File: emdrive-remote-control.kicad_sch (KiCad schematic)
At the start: 44 parts, among them J1 Raspberry_Pi_2_3, J2 Screw_Terminal_01x06, J3 Conn_01x04, J4 Screw_Terminal_01x06, K1 Relay_SPST-NO, Q1 DMN61D8LQ, SW3 SW_Push, SW4 SW_Push, U1 ADS1015IDGS, U2 WS2801SO, U3 AP62150WU, U5 SN74HCS125, U6 MCP602, U7 BTS6143D

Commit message: Continues SCH, placed components on PCB
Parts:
- removed J4: Screw_Terminal_01x06, PrivateLibrary:Terminal_Block_SERIES 4115_5.08_Spring_6POS, symbol Connector:Screw_Terminal_01x06
- added Q2: MMBT3904, Package_TO_SOT_SMD:SOT-23, symbol Transistor_BJT:MMBT3904
- added R11, R12, R17, R18: 33k, Resistor_SMD:R_0603_1608Metric_Pad0.98x0.95mm_HandSolder, symbol Device:R
- renumbered SW3 to SW1, SW4 to SW2
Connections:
- net +12L: no longer K1.14
- net +12V: now also J2.1 (Pin_1), U7.3 (Vbb); no longer K1.13
- net +3.3V: now also J1.1 (3V3), J1.17 (3V3)
- net +5V: now also J1.2 (5V), J1.4 (5V)
- net GND: now also C10.1, C11.1, C12.1, C6.1, J1.14 (GND), J1.20 (GND), J1.25 (GND), J1.30 (GND), J1.34 (GND), J1.39 (GND), J1.6 (GND), J1.9 (GND), J2.2 (Pin_2), J2.4 (Pin_4), R16.2, U1.1 (ADDR), U1.3 (GND), U6.4 (V-), Q2.2 (E), R11.2, R18.2
- net GNDA: no longer C10.1, C11.1, C12.1, C6.1, U1.1 (ADDR), U1.3 (GND), U6.4 (V-)
- net WDT_P1: now also J2.5 (Pin_5), K1.14
- net WDT_P2: now also J2.6 (Pin_6), K1.13
- net I_SENSE: now reaches R14.2
- net I_SENSE: now also U7.4 (IS), R11.1
- net BTN_2: now reaches R8.1, SW2.1
- net BTN_2: now also J1.29 (GCLK1/GPIO5)
- net at J2.3 (Pin_3): now also U7.1 (OUT), U7.5 (OUT)
- net IN_LED_R: now reaches J1.15 (GPIO22)
- net IN_LED_R: now also U5.3 (Y1)
- net IN_LED_G: now reaches J1.16 (GPIO23)
- net IN_LED_G: now also U5.6 (Y2)
- net IN_LED_Y: now reaches J1.18 (GPIO24)
- net IN_LED_Y: now also U5.8 (Y3)
- net SPI_MOSI: now reaches J1.19 (MOSI0/GPIO10)
- net SPI_MOSI: now also U2.2 (SDI)
- net SPI_SCLK: now reaches J1.23 (SCLK0/GPIO11)
- net SPI_SCLK: now also U2.1 (CKI)
- net WDT_EN: now reaches J1.26 (~{CE1}/GPIO7)
- net WDT_EN: now also Q1.1 (G), R6.2
- net I2C_SDA: now reaches J1.3 (SDA/GPIO2)
- net I2C_SDA: now also R10.2, U1.9 (SDA), U4.4 (SDA)
- net DRIVE_PS_EN: now reaches J1.31 (GCLK2/GPIO6)
- net DRIVE_PS_EN: now also R17.1
- net I2C_SCL: now reaches J1.5 (SCL/GPIO3)
- net I2C_SCL: now also R9.2, U1.10 (SCL), U4.3 (SCK)
- net BTN_1: now reaches J1.7 (GCLK0/GPIO4)
- net BTN_1: now also R7.1, SW1.1
- net at U7.2 (IN): now also R12.1
- new net: Q2.1 (B), R17.2, R18.1
- new net: Q2.3 (C), R12.2
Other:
- moved on the sheet: C10, C11, C12, C2, C3, C4, C5, C6, C8, FB1, J1, J2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

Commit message: Initial Routing. Minor modifications to .sch. SCH verified.
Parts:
- added D3, D4: LED, LED_SMD:LED_0805_2012Metric, symbol Device:LED
- added H1: MountingHole, MountingHole:MountingHole_3.2mm_M3_DIN965, symbol Mechanical:MountingHole
- added R19, R20: 0R, Resistor_SMD:R_0603_1608Metric_Pad0.98x0.95mm_HandSolder, symbol Device:R
- added R21: 220R, Resistor_SMD:R_0603_1608Metric_Pad0.98x0.95mm_HandSolder, symbol Device:R
- added R22: 1k, Resistor_SMD:R_0603_1608Metric_Pad0.98x0.95mm_HandSolder, symbol Device:R
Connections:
- net +12V: now also R22.2
- net +5V: now also R21.2
- net GND: now also D3.1 (K), D4.1 (K), R19.1, R20.1; no longer U1.1 (ADDR)
- net WDT_EN: now also R19.2
- new net: D4.2 (A), R22.1
- new net: D3.2 (A), R21.1
- new net: R20.2, U1.1 (ADDR)
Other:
- note added: "Buttons"
- note added: "GPIO Input"
- note added: "Watchdog Relay"
- moved on the sheet: C10, C11, C12, C2, C3, C4, C5, C6, C7, C8, D1, FB1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

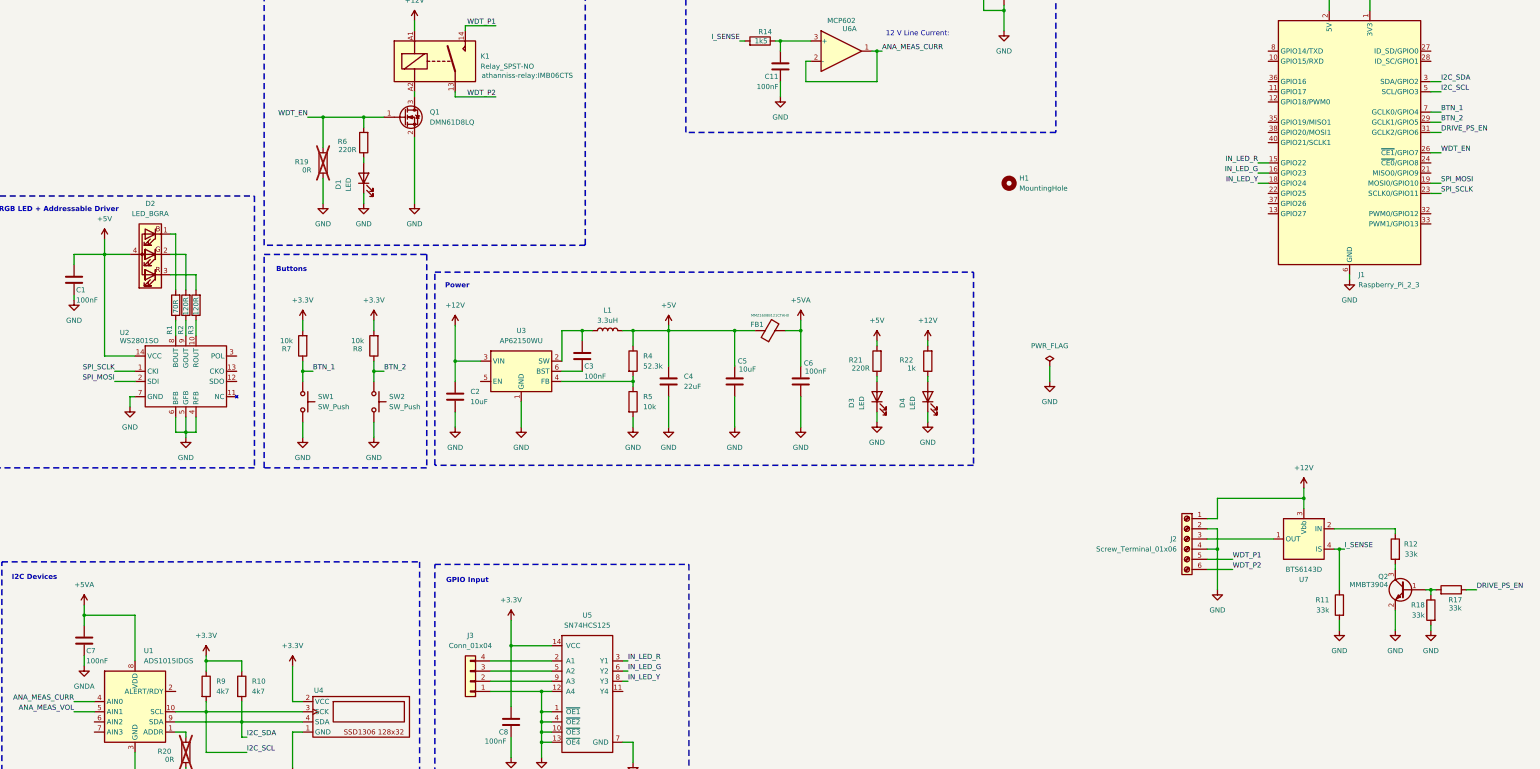
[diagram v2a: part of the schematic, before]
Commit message: Moved around modules on the PCB. Minor fixes in SCH.
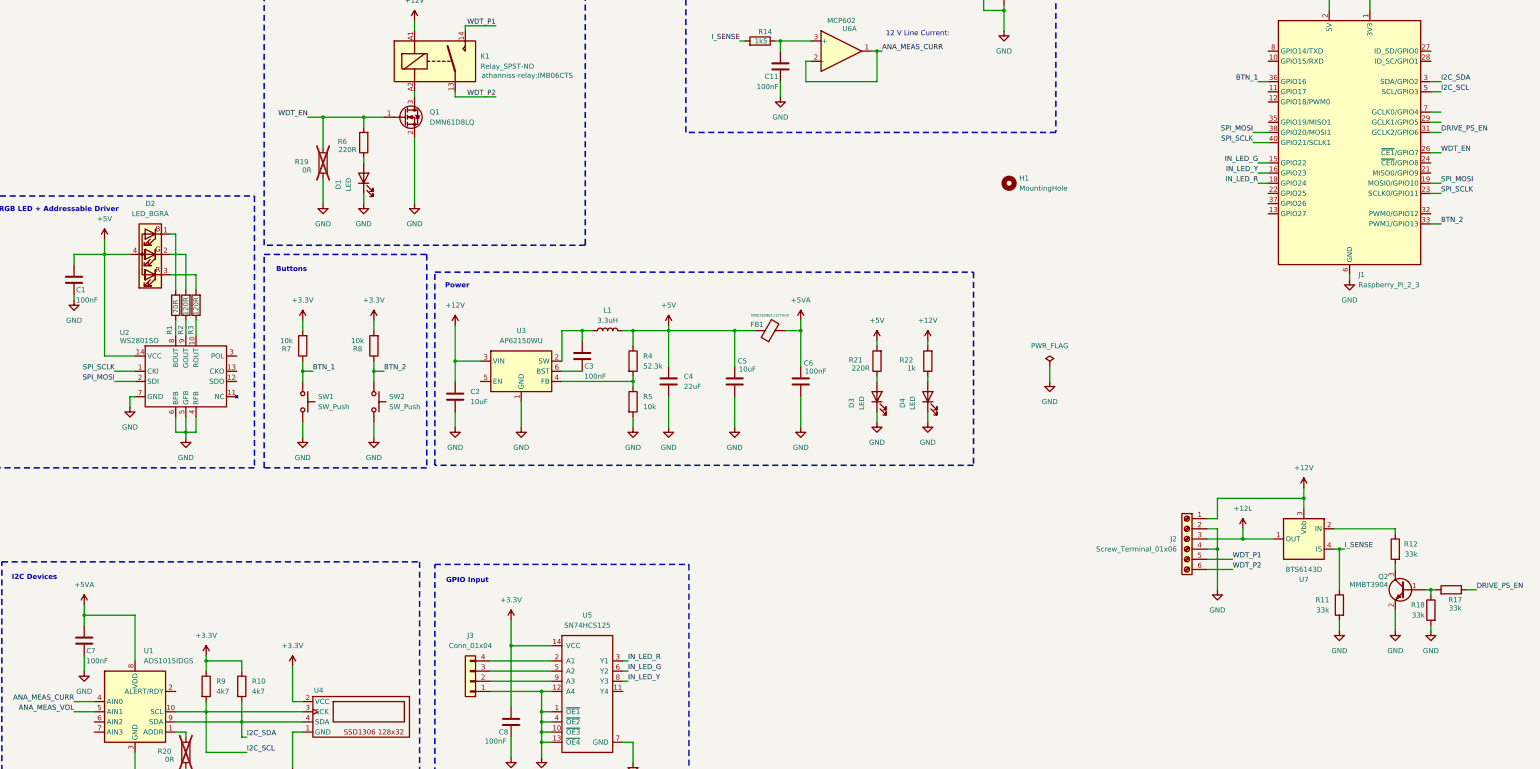
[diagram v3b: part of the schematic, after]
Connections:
- net GNDA is gone; now on net GND: C7.1
- net +12L: now also J2.3 (Pin_3), U7.1 (OUT), U7.5 (OUT)
- net BTN_1: now also J1.36 (GPIO16); no longer J1.7 (GCLK0/GPIO4)
- net BTN_2: now also J1.33 (PWM1/GPIO13); no longer J1.29 (GCLK1/GPIO5)
- net IN_LED_G: now also J1.15 (GPIO22); no longer J1.16 (GPIO23)
- net IN_LED_R: now also J1.18 (GPIO24); no longer J1.15 (GPIO22)
- net IN_LED_Y: now also J1.16 (GPIO23); no longer J1.18 (GPIO24)
- net SPI_MOSI: now also J1.38 (GPIO20/MOSI1)
- net SPI_SCLK: now also J1.40 (GPIO21/SCLK1)
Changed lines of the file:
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@@
 	)
 	(junction
+		(at 328.93 212.09)
+		(diameter 0)
+		(color 0 0 0 0)
+	)
+	(junction
 		(at 111.76 170.18)
 		(diameter 0)
@@
 	(wire
 		(pts
+			(xy 331.47 110.49) (xy 335.28 110.49)
+		)
+		(stroke
+			(width 0)
+			(type default)
+		)
+	)
+	(wire
+		(pts
 			(xy 344.17 201.93) (xy 344.17 204.47)
 		)
@@
 	(wire
 		(pts
+			(xy 375.92 133.35) (xy 378.46 133.35)
+		)
+		(stroke
+			(width 0)
+			(type default)
+		)
+	)
+	(wire
+		(pts
 			(xy 344.17 199.39) (xy 344.17 201.93)
 		)
@@
 	(wire
 		(pts
+			(xy 39.37 241.3) (xy 39.37 245.11)
+		)
+		(stroke
+			(width 0)
+			(type default)
+		)
+	)
+	(wire
+		(pts
 			(xy 140.97 242.57) (xy 156.21 242.57)
 		)
@@
 	(wire
 		(pts
+			(xy 332.74 97.79) (xy 335.28 97.79)
+		)
+		(stroke
+			(width 0)
+			(type default)
+		)
+	)
+	(wire
+		(pts
 			(xy 375.92 123.19) (xy 378.46 123.19)
 		)
@@
 	(wire
 		(pts
+			(xy 331.47 113.03) (xy 335.28 113.03)
+		)
+		(stroke
+			(width 0)
+			(type default)
+		)
+	)
+	(wire
+		(pts
 			(xy 320.04 209.55) (xy 322.58 209.55)
 		)
@@
 	(wire
 		(pts
+			(xy 328.93 212.09) (xy 320.04 212.09)
+		)
+		(stroke
+			(width 0)
+			(type default)
+		)
+	)
+	(wire
+		(pts
 			(xy 176.53 171.45) (xy 176.53 172.72)
 		)
@@
 	(wire
 		(pts
-			(xy 336.55 212.09) (xy 320.04 212.09)
+			(xy 336.55 212.09) (xy 328.93 212.09)
 		)
 		(stroke
@@
 	(wire
 		(pts
-			(xy 39.37 241.3) (xy 39.37 243.84)
-		)
-		(stroke
-			(width 0)
-			(type default)
-		)
-	)
-	(wire
-		(pts
 			(xy 78.74 257.81) (xy 93.98 257.81)
 		)
@@
 	(wire
 		(pts
+			(xy 328.93 209.55) (xy 328.93 212.09)
+		)
+		(stroke
+			(width 0)
+			(type default)
+		)
+	)
+	(wire
+		(pts
 			(xy 220.98 58.42) (xy 215.9 58.42)
 		)
@@
 	)
 	(label "IN_LED_R"
-		(at 332.74 118.11 180)
+		(at 332.74 123.19 180)
 		(fields_autoplaced yes)
 		(effects
@@
 	)
 	(label "IN_LED_G"
-		(at 332.74 120.65 180)
+		(at 332.74 118.11 180)
 		(fields_autoplaced yes)
 		(effects
@@
 	)
 	(label "BTN_2"
-		(at 378.46 107.95 0)
+		(at 378.46 133.35 0)
 		(fields_autoplaced yes)
 		(effects
@@
 	)
 	(label "IN_LED_Y"
-		(at 332.74 123.19 180)
+		(at 332.74 120.65 180)
 		(fields_autoplaced yes)
 		(effects
@@
 		)
 	)
+	(label "SPI_MOSI"
+		(at 331.47 110.49 180)
+		(fields_autoplaced yes)
+		(effects
+			(font
+				(size 1.27 1.27)
+			)
+			(justify right bottom)
+		)
+	)
+	(label "SPI_SCLK"
+		(at 331.47 113.03 180)
+		(fields_autoplaced yes)
+		(effects
+			(font
+				(size 1.27 1.27)
+			)
+			(justify right bottom)
+		)
+	)
 	(label "IN_LED_G"
 		(at 175.26 245.11 0)
@@
 	)
 	(label "BTN_1"
-		(at 378.46 105.41 0)
+		(at 332.74 97.79 180)
 		(fields_autoplaced yes)
 		(effects
@@
 				(size 1.27 1.27)
 			)
-			(justify left bottom)
+			(justify right bottom)
 		)
 	)
@@
 	)
 	(symbol
+		(lib_id "power:+12L")
+		(at 328.93 209.55 0)
+		(mirror y)
+		(unit 1)
+		(exclude_from_sim no)
+		(in_bom yes)
+		(on_board yes)
+		(dnp no)
+		(fields_autoplaced yes)
+		(property "Reference" "#PWR052"
+			(at 328.93 213.36 0)
+			(effects
+				(font
+					(size 1.27 1.27)
+				)
+				(hide yes)
+			)
+		)
+		(property "Value" "+12L"
+			(at 328.93 204.47 0)
+			(effects
+				(font
+					(size 1.27 1.27)
+				)
+			)
+		)
+		(property "Footprint" ""
+			(at 328.93 209.55 0)
+			(effects
+				(font
+					(size 1.27 1.27)
+				)
+				(hide yes)
+			)
+		)
+		(property "Datasheet" ""
+			(at 328.93 209.55 0)
+			(effects
+				(font
+					(size 1.27 1.27)
+				)
+				(hide yes)
+			)
+		)
+		(property "Description" "Power symbol creates a global label with name \"+12L\""
+			(at 328.93 209.55 0)
+			(effects
+				(font
+					(size 1.27 1.27)
+				)
+				(hide yes)
+			)
+		)
+		(pin "1"
+		)
+		(instances
+			(project "emdrive-remote-control"
+				(path "/9dab341a-1f04-42ca-8245-31cf01963ea8"
+					(reference "#PWR052")
+					(unit 1)
+				)
+			)
+		)
+	)
+	(symbol
 		(lib_id "Device:C")
 		(at 39.37 237.49 180)
@@
 	)
 	(symbol
-		(lib_id "power:GNDA")
-		(at 39.37 243.84 0)
-		(unit 1)
-		(exclude_from_sim no)
-		(in_bom yes)
-		(on_board yes)
-		(dnp no)
-		(fields_autoplaced yes)
-		(property "Reference" "#PWR024"
-			(at 39.37 250.19 0)
-			(effects
-				(font
-					(size 1.27 1.27)
-				)
-				(hide yes)
-			)
-		)
-		(property "Value" "GNDA"
-			(at 39.37 248.92 0)
-			(effects
-				(font
-					(size 1.27 1.27)
-				)
-			)
-		)
-		(property "Footprint" ""
-			(at 39.37 243.84 0)
-			(effects
-				(font
-					(size 1.27 1.27)
-				)
-				(hide yes)
-			)
-		)
-		(property "Datasheet" ""
-			(at 39.37 243.84 0)
-			(effects
-				(font
-					(size 1.27 1.27)
-				)
-				(hide yes)
-			)
-		)
-		(property "Description" "Power symbol creates a global label with name \"GNDA\" , analog ground"
-			(at 39.37 243.84 0)
-			(effects
-				(font
-					(size 1.27 1.27)
-				)
-				(hide yes)
-			)
-		)
-		(pin "1"
-		)
-		(instances
-			(project "emdrive-remote-control"
-				(path "/9dab341a-1f04-42ca-8245-31cf01963ea8"
-					(reference "#PWR024")
-					(unit 1)
-				)
-			)
-		)
-	)
-	(symbol
 		(lib_id "power:GND")
 		(at 185.42 184.15 0)
@@
 					(unit 1)
 				)
+			)
+		)
+	)
+	(symbol
+		(lib_id "power:GND")
+		(at 39.37 245.11 0)
+		(unit 1)
+		(exclude_from_sim no)
+		(in_bom yes)
+		(on_board yes)
+		(dnp no)
+		(fields_autoplaced yes)
+		(property "Reference" "#PWR024"
+			(at 39.37 251.46 0)
+			(effects
+				(font
+					(size 1.27 1.27)
+				)
+				(hide yes)
+			)
+		)
+		(property "Value" "GND"
+			(at 39.37 250.19 0)
+			(effects
+				(font
+					(size 1.27 1.27)
+				)
+			)
+		)
+		(property "Footprint" ""
+			(at 39.37 245.11 0)
+			(effects
+				(font
+					(size 1.27 1.27)
+				)
+				(hide yes)
+			)
+		)
+		(property "Datasheet" ""
+			(at 39.37 245.11 0)
+			(effects
+				(font
+					(size 1.27 1.27)
+				)
+				(hide yes)
+			)
+		)
+		(property "Description" "Power symbol creates a global label with name \"GND\" , ground"
+			(at 39.37 245.11 0)
+			(effects
+				(font
+					(size 1.27 1.27)
+				)
+				(hide yes)
+			)
+		)
+		(pin "1"
+		)
+		(instances
+			(project "emdrive-remote-control"
+				(path "/9dab341a-1f04-42ca-8245-31cf01963ea8"
+					(reference "#PWR024")
+					(unit 1)
+				)
